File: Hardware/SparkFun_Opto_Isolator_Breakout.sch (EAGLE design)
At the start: 16 parts, among them Q1 NPN, Q2 NPN, U1 OPTOISOLATOR-2SOIC8

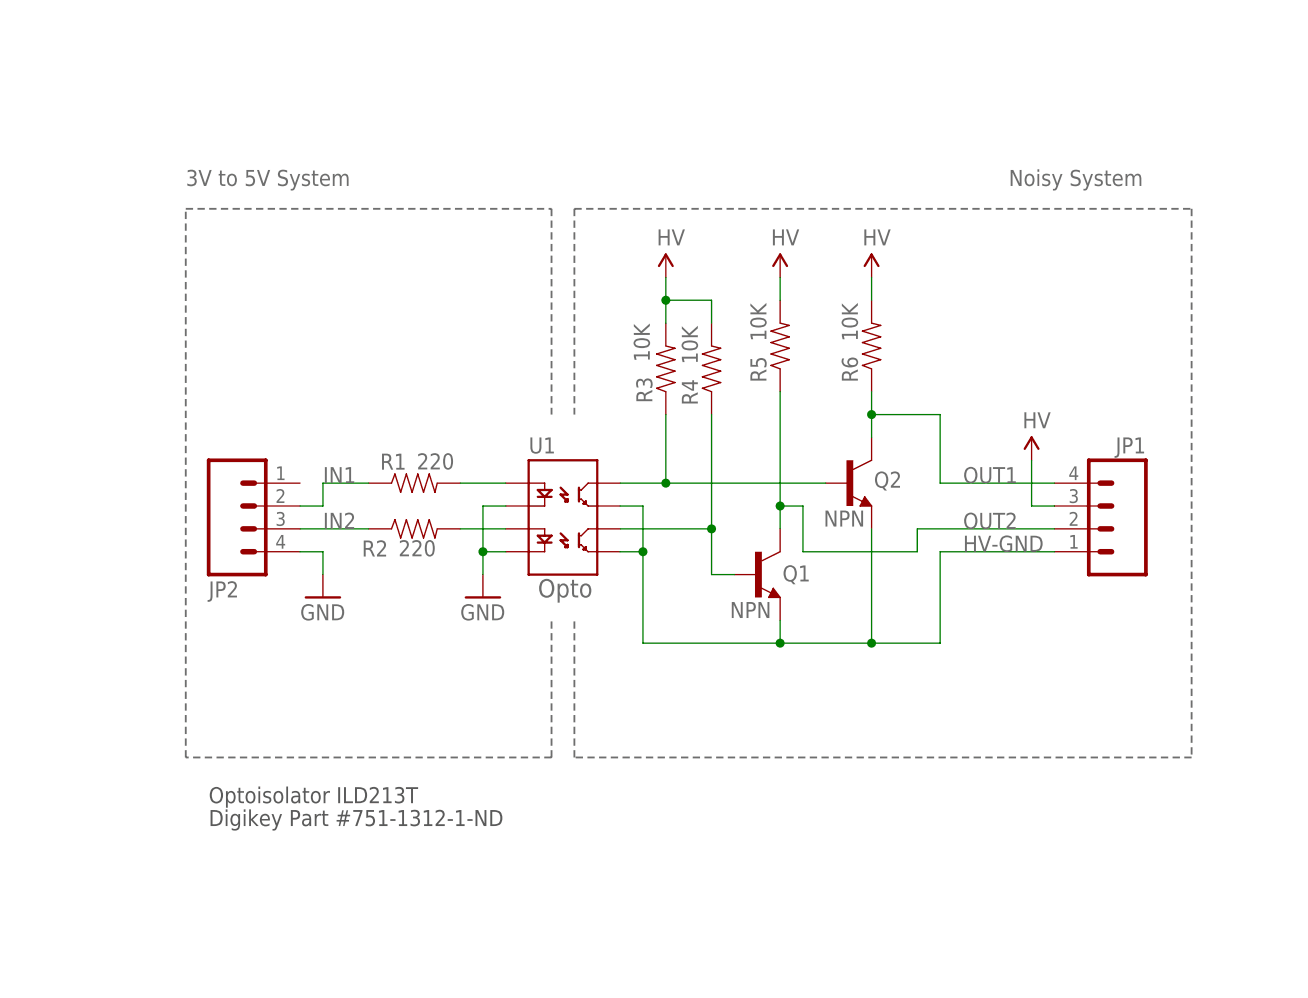
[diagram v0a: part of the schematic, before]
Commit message: Replace ILD213T with updated part
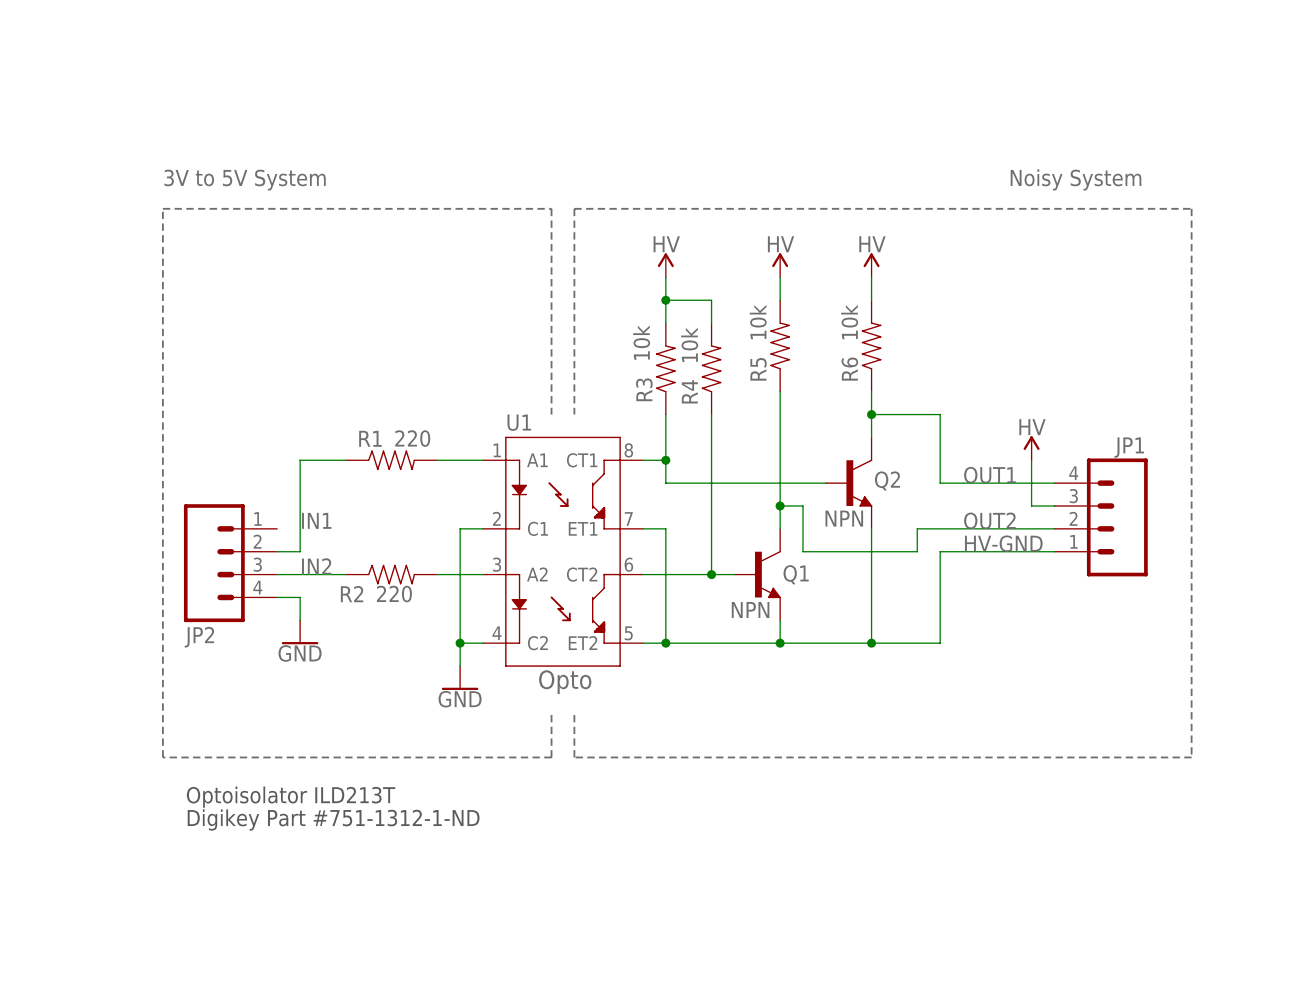
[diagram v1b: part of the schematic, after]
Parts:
- R1, R2: device SparkFun-Resistors:220OHM-1/10W-1%(0603) -> SparkFun-Resistors:220OHM-0603-1/10W-1%
- R3, R4, R5, R6: value 10K -> 10k; device SparkFun-Resistors:10KOHM1/10W1%(0603)0603 -> SparkFun-Resistors:10KOHM-0603-1/10W-1%
- U1: value OPTOISOLATOR-2SOIC8 -> ILD213T-IDL213T; device SparkFun-DiscreteSemi:OPTOISOLATOR-2SOIC8 -> SparkFun-DiscreteSemi:ILD213T-IDL213T
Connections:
- net HV-GND: now also U1.ET1, U1.ET2; no longer U1.EM1, U1.EM2
- net OUT1N: now also U1.CT1; no longer U1.CL1
- net OUT2N: now also U1.CT2; no longer U1.CL2
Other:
- moved on the sheet: JP2, R1, R2
